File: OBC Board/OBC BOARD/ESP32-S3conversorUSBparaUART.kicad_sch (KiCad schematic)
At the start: 12 parts, among them J1 USB_B_Micro, J2 USB_B_Micro

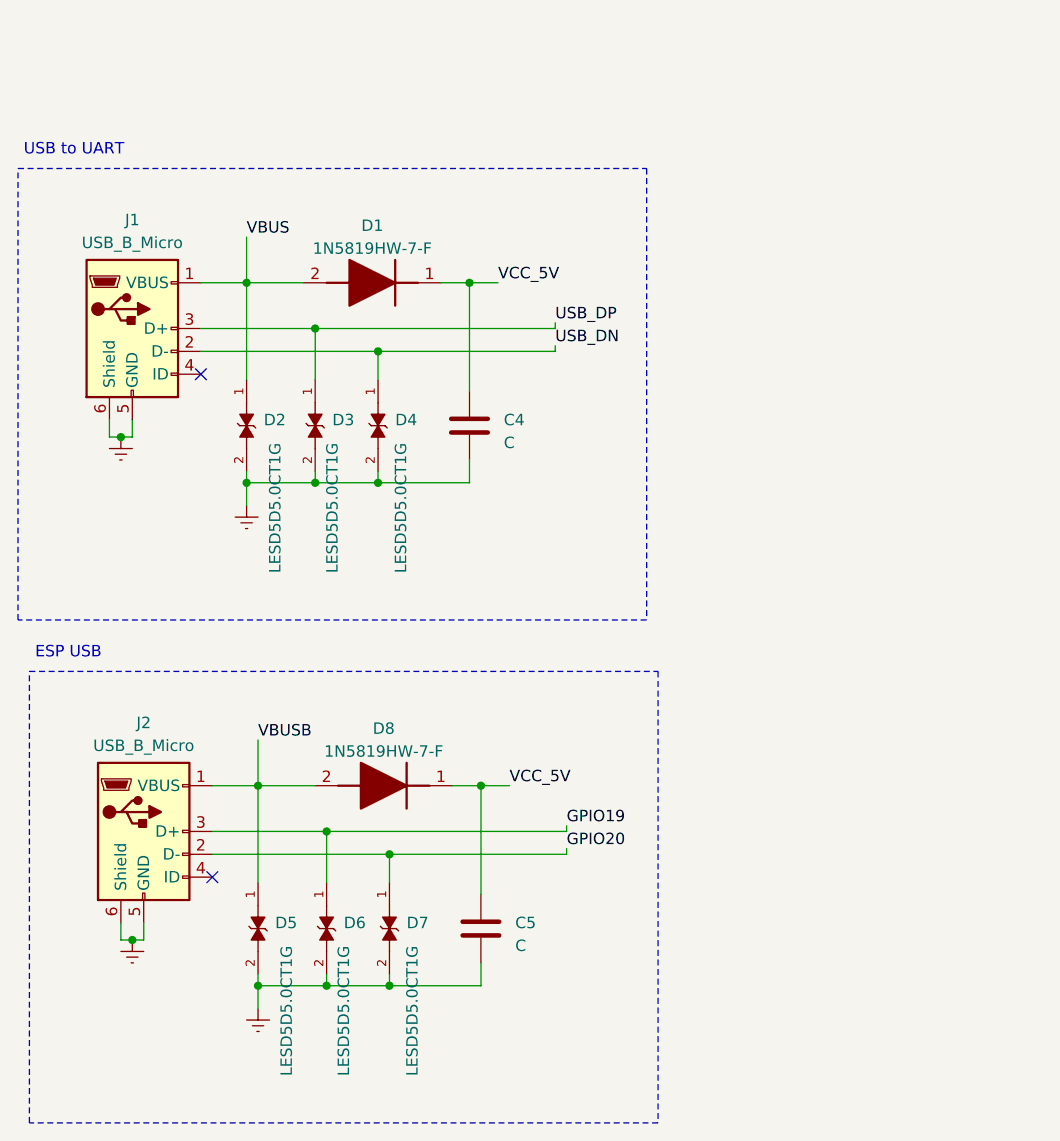
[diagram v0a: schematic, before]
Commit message: Realização do diagrama de blocos, test points, padronização e mudança dos caminhos das bibliotecas de footprints e simbolos
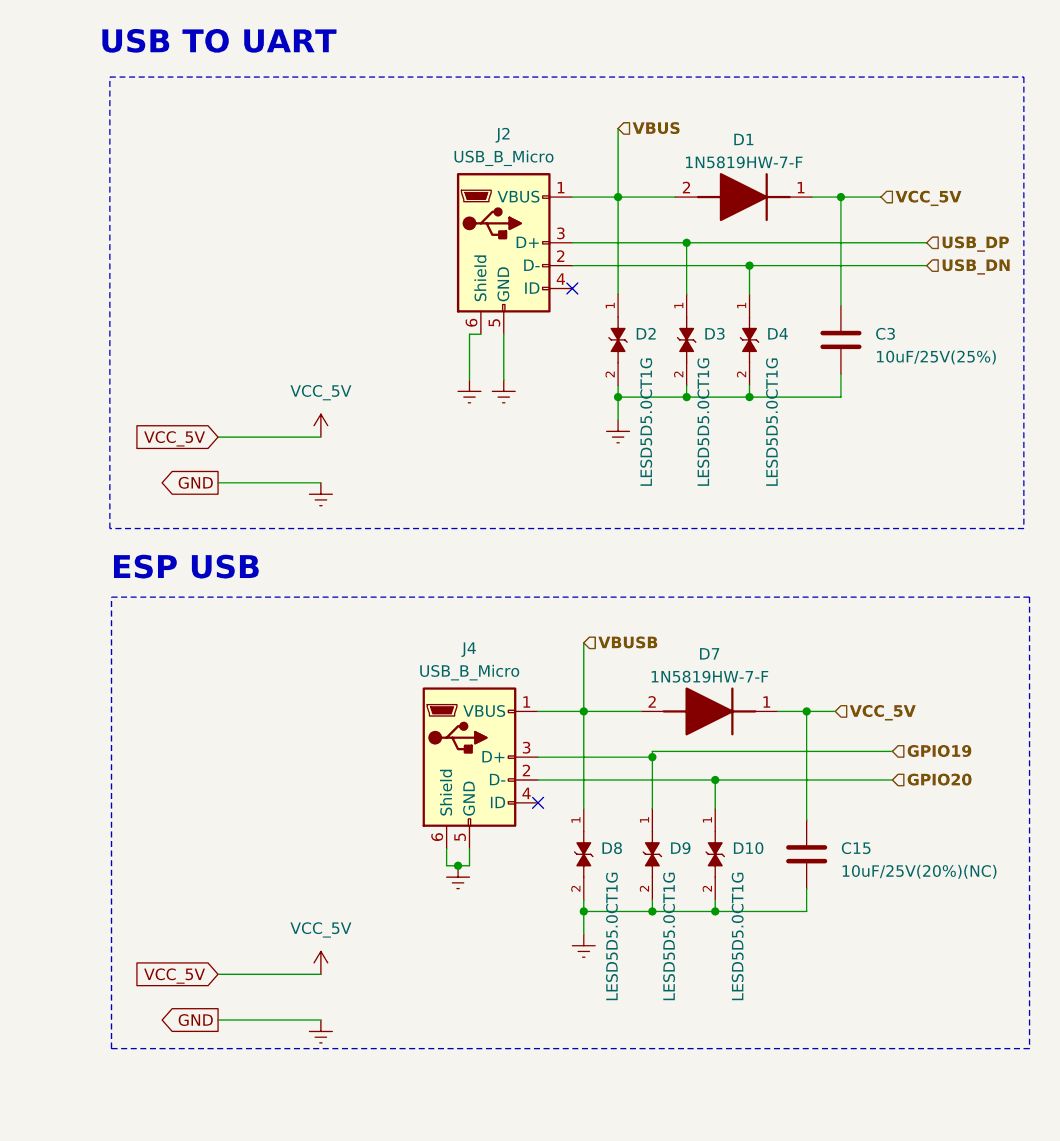
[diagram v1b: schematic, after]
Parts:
- C15: renamed from C5; value C -> 10uF/25V(20%)(NC); footprint (none) -> Capacitor_SMD:C_0402_1005Metric
- C3: renamed from C4; value C -> 10uF/25V(25%); footprint (none) -> Capacitor_SMD:C_0402_1005Metric
- D1: footprint SOD3716X145N -> SOD3716X145N:SOD3716X145N
- D10: renamed from D7; footprint LESD5D5.0CT1G:TVS_LESD5D5.0CT1G -> TVS_LESD5D5.0CT1G:TVS_LESD5D5.0CT1G
- D2, D3, D4: footprint LESD5D5.0CT1G:TVS_LESD5D5.0CT1G -> TVS_LESD5D5.0CT1G:TVS_LESD5D5.0CT1G
- D7: renamed from D8; footprint SOD3716X145N -> SOD3716X145N:SOD3716X145N
- D8: renamed from D5; footprint LESD5D5.0CT1G:TVS_LESD5D5.0CT1G -> TVS_LESD5D5.0CT1G:TVS_LESD5D5.0CT1G
- D9: renamed from D6; footprint LESD5D5.0CT1G:TVS_LESD5D5.0CT1G -> TVS_LESD5D5.0CT1G:TVS_LESD5D5.0CT1G
- J2: renamed from J1; footprint (none) -> Connector_USB:USB_Micro-AB_Molex_47590-0001
- J4: renamed from J2; footprint (none) -> Connector_USB:USB_Micro-AB_Molex_47590-0001
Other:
- note added: "USB TO UART"
- note removed: "USB to UART"
- title: ICARUS-2 OBCH -> ICARUS-2 OBDH
- moved on the sheet: C15, C3, D1, D10, D2, D3, D4, D7, D8, D9, J2, J4

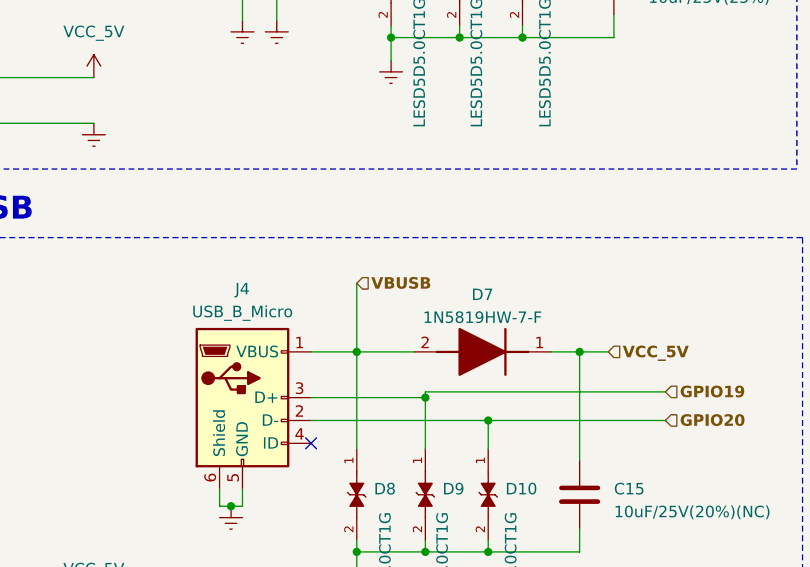
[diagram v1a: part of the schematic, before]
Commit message: Junção dos projetos FPGA e ESP32. Biblioteca de simbolos e footprints realizadas. Definição do caminho para os arquivos. Inclusão do esquema librecube.
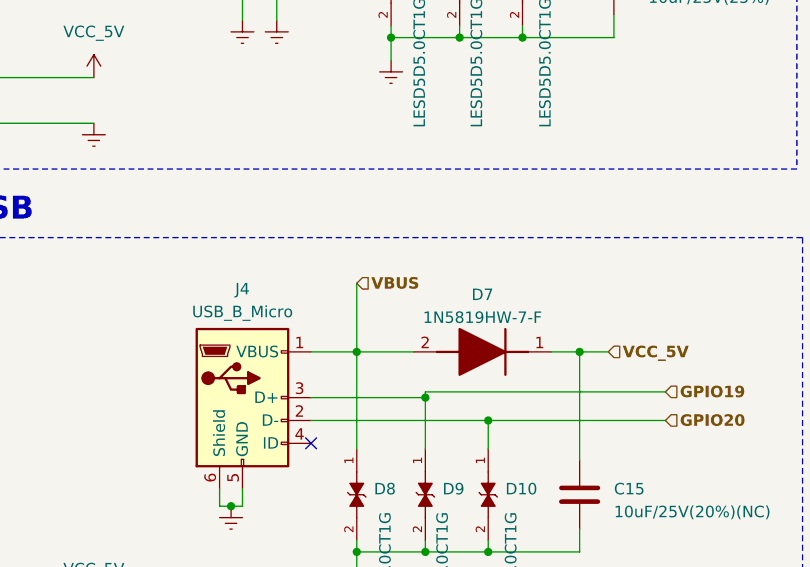
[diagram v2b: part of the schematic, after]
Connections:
- net VBUSB is gone; now on net VBUS: D7.2 (A), D8.1, J4.1 (VBUS)
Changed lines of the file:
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@@
 	(title_block
 		(title "ICARUS-2 OBDH")
-		(date "2024-03-15")
+		(date "2024-03-24")
 		(rev "POC 2.0")
 		(comment 2 "WILLIAN BUENO SANTOS")
@@
 		)
 	)
-	(hierarchical_label "VBUSB"
+	(hierarchical_label "VBUS"
 		(shape input)
 		(at 143.51 99.06 0)
